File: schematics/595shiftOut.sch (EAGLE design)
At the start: 7 parts, among them IC1 74HC595N, IC2 74HC595N, U1 TINY45-20-DIP

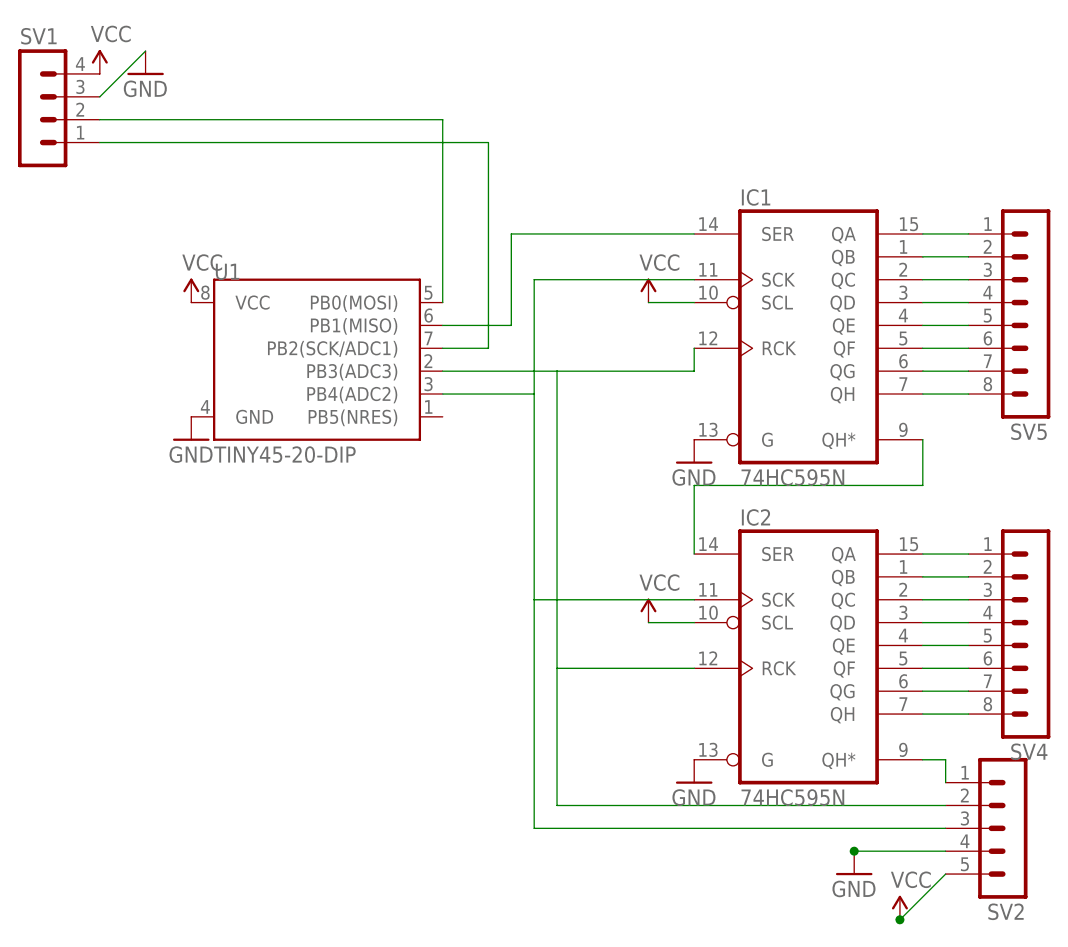
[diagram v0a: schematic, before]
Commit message: rework the schematics for cnc milling
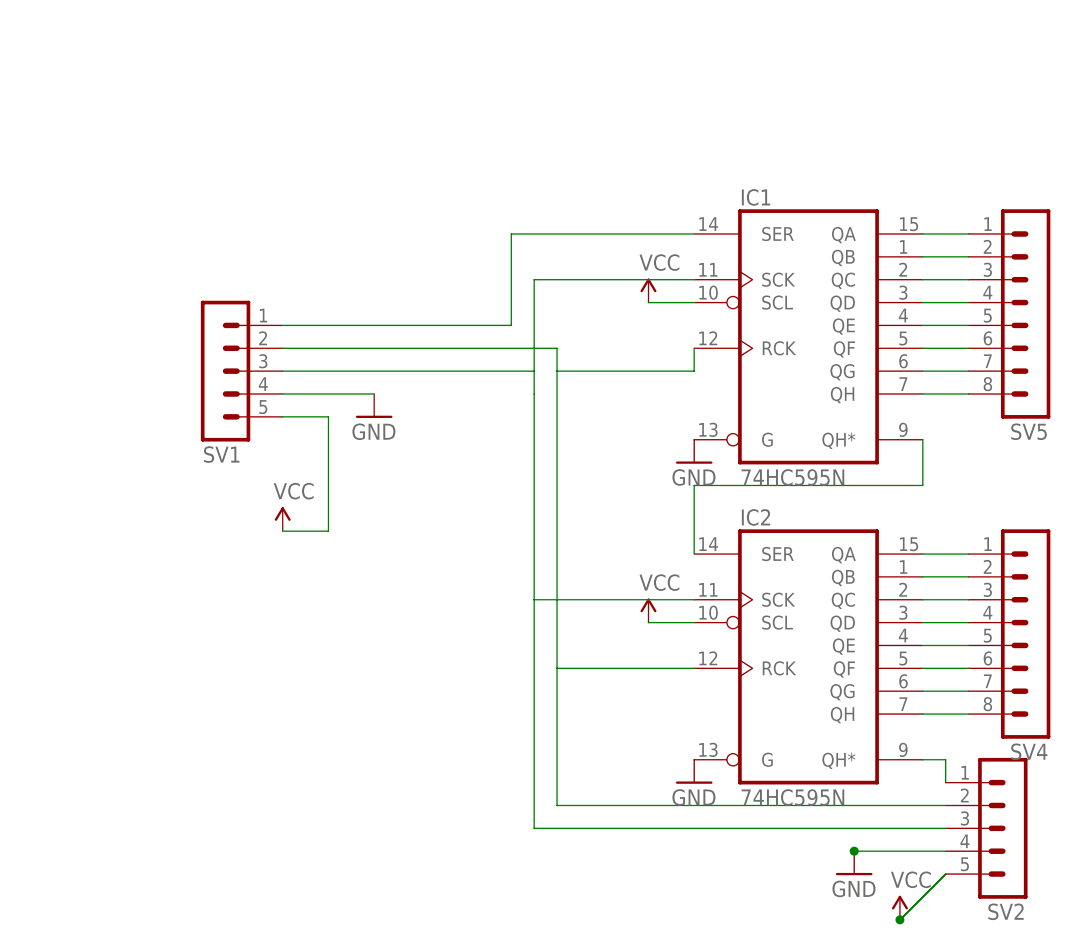
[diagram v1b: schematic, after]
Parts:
- removed U1: TINY45-20-DIP, SparkFun-DigitalIC:ATTINY45TINY45-20-DIP
- SV1: device con-lstb:MA04-1 -> con-lstb:MA05-1
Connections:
- removed net N$1: SV1.2, U1.PB0(MOSI)
- removed net N$2: SV1.1, U1.PB2(SCK/ADC1)
- net GND: now also SV1.4; no longer SV1.3, U1.GND
- net N$3: now also SV1.1; no longer U1.PB1(MISO)
- net N$4: now also SV1.2; no longer U1.PB3(ADC3)
- net N$5: now also SV1.3; no longer U1.PB4(ADC2)
- net VCC: now also SV1.5; no longer SV1.4, U1.VCC
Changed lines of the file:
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@@
 <?xml version="1.0" encoding="utf-8"?>
 <!DOCTYPE eagle SYSTEM "eagle.dtd">
-<eagle version="6.4">
+<eagle version="7.3.0">
 <drawing>
 <settings>
@@
 </classes>
 <parts>
-<part name="U1" library="SparkFun-DigitalIC" deviceset="ATTINY45" device="TINY45-20-DIP" value="TINY45-20-DIP"/>
-<part name="SUPPLY1" library="SparkFun-Aesthetics" deviceset="VCC" device=""/>
-<part name="GND1" library="SparkFun-Aesthetics" deviceset="GND" device=""/>
-<part name="SV1" library="con-lstb" deviceset="MA04-1" device=""/>
-<part name="SUPPLY2" library="SparkFun-Aesthetics" deviceset="VCC" device=""/>
-<part name="GND2" library="SparkFun-Aesthetics" deviceset="GND" device=""/>
 <part name="IC1" library="74xx-eu" deviceset="74*595" device="N" technology="HC"/>
 <part name="IC2" library="74xx-eu" deviceset="74*595" device="N" technology="HC"/>
@@
 <part name="GND5" library="SparkFun-Aesthetics" deviceset="GND" device=""/>
 <part name="SUPPLY5" library="SparkFun-Aesthetics" deviceset="VCC" device=""/>
+<part name="SV1" library="con-lstb" deviceset="MA05-1" device=""/>
+<part name="GND1" library="SparkFun-Aesthetics" deviceset="GND" device=""/>
+<part name="SUPPLY1" library="SparkFun-Aesthetics" deviceset="VCC" device=""/>
 </parts>
 <sheets>
@@
 </plain>
 <instances>
-<instance part="U1" gate="G$1" x="35.56" y="30.48"/>
-<instance part="SUPPLY1" gate="1" x="20.32" y="38.1"/>
-<instance part="GND1" gate="1" x="20.32" y="22.86"/>
-<instance part="SV1" gate="1" x="2.54" y="60.96"/>
-<instance part="SUPPLY2" gate="1" x="10.16" y="63.5"/>
-<instance part="GND2" gate="1" x="15.24" y="63.5"/>
 <instance part="IC1" gate="A" x="88.9" y="35.56"/>
 <instance part="IC2" gate="A" x="88.9" y="0"/>
@@
 <instance part="GND5" gate="1" x="93.98" y="-25.4"/>
 <instance part="SUPPLY5" gate="1" x="99.06" y="-30.48"/>
+<instance part="SV1" gate="G$1" x="22.86" y="30.48" rot="MR180"/>
+<instance part="GND1" gate="1" x="40.64" y="25.4"/>
+<instance part="SUPPLY1" gate="1" x="30.48" y="12.7"/>
 </instances>
 <busses>
@@
 <net name="VCC" class="0">
 <segment>
-<pinref part="U1" gate="G$1" pin="VCC"/>
-<pinref part="SUPPLY1" gate="1" pin="VCC"/>
-</segment>
-<segment>
-<pinref part="SV1" gate="1" pin="4"/>
-<pinref part="SUPPLY2" gate="1" pin="VCC"/>
-</segment>
-<segment>
 <pinref part="IC1" gate="A" pin="SCL"/>
 <pinref part="SUPPLY3" gate="1" pin="VCC"/>
@@
 <pinref part="SUPPLY5" gate="1" pin="VCC"/>
 <wire x1="99.06" y1="-30.48" x2="104.14" y2="-25.4" width="0.1524" layer="91"/>
+<wire x1="99.06" y1="-30.48" x2="104.14" y2="-25.4" width="0.1524" layer="91"/>
+<wire x1="99.06" y1="-30.48" x2="104.14" y2="-25.4" width="0.1524" layer="91"/>
+<wire x1="99.06" y1="-30.48" x2="104.14" y2="-25.4" width="0.1524" layer="91"/>
+</segment>
+<segment>
+<pinref part="SV1" gate="G$1" pin="5"/>
+<wire x1="30.48" y1="25.4" x2="35.56" y2="25.4" width="0.1524" layer="91"/>
+<wire x1="35.56" y1="25.4" x2="35.56" y2="12.7" width="0.1524" layer="91"/>
+<pinref part="SUPPLY1" gate="1" pin="VCC"/>
+<wire x1="35.56" y1="12.7" x2="30.48" y2="12.7" width="0.1524" layer="91"/>
 </segment>
 </net>
 <net name="GND" class="0">
-<segment>
-<pinref part="U1" gate="G$1" pin="GND"/>
-<pinref part="GND1" gate="1" pin="GND"/>
-</segment>
-<segment>
-<pinref part="SV1" gate="1" pin="3"/>
-<pinref part="GND2" gate="1" pin="GND"/>
-<wire x1="15.24" y1="66.04" x2="10.16" y2="60.96" width="0.1524" layer="91"/>
-</segment>
 <segment>
 <pinref part="IC2" gate="A" pin="G"/>
@@
 <wire x1="93.98" y1="-22.86" x2="104.14" y2="-22.86" width="0.1524" layer="91"/>
 </segment>
-</net>
-<net name="N$1" class="0">
-<segment>
-<pinref part="SV1" gate="1" pin="2"/>
-<pinref part="U1" gate="G$1" pin="PB0(MOSI)"/>
-<wire x1="10.16" y1="58.42" x2="48.26" y2="58.42" width="0.1524" layer="91"/>
-<wire x1="48.26" y1="58.42" x2="48.26" y2="38.1" width="0.1524" layer="91"/>
-</segment>
-</net>
-<net name="N$2" class="0">
-<segment>
-<pinref part="SV1" gate="1" pin="1"/>
-<wire x1="10.16" y1="55.88" x2="53.34" y2="55.88" width="0.1524" layer="91"/>
-<wire x1="53.34" y1="55.88" x2="53.34" y2="33.02" width="0.1524" layer="91"/>
-<pinref part="U1" gate="G$1" pin="PB2(SCK/ADC1)"/>
-<wire x1="53.34" y1="33.02" x2="48.26" y2="33.02" width="0.1524" layer="91"/>
+<segment>
+<pinref part="SV1" gate="G$1" pin="4"/>
+<pinref part="GND1" gate="1" pin="GND"/>
+<wire x1="30.48" y1="27.94" x2="40.64" y2="27.94" width="0.1524" layer="91"/>
 </segment>
 </net>
 <net name="N$3" class="0">
 <segment>
-<pinref part="U1" gate="G$1" pin="PB1(MISO)"/>
-<wire x1="48.26" y1="35.56" x2="55.88" y2="35.56" width="0.1524" layer="91"/>
+<wire x1="30.48" y1="35.56" x2="55.88" y2="35.56" width="0.1524" layer="91"/>
 <wire x1="55.88" y1="35.56" x2="55.88" y2="45.72" width="0.1524" layer="91"/>
 <pinref part="IC1" gate="A" pin="SER"/>
 <wire x1="55.88" y1="45.72" x2="76.2" y2="45.72" width="0.1524" layer="91"/>
+<pinref part="SV1" gate="G$1" pin="1"/>
 </segment>
 </net>
 <net name="N$4" class="0">
 <segment>
-<pinref part="U1" gate="G$1" pin="PB3(ADC3)"/>
 <pinref part="IC1" gate="A" pin="RCK"/>
-<wire x1="48.26" y1="30.48" x2="60.96" y2="30.48" width="0.1524" layer="91"/>
+<wire x1="60.96" y1="33.02" x2="60.96" y2="30.48" width="0.1524" layer="91"/>
 <wire x1="60.96" y1="30.48" x2="76.2" y2="30.48" width="0.1524" layer="91"/>
 <wire x1="76.2" y1="30.48" x2="76.2" y2="33.02" width="0.1524" layer="91"/>
@@
 <wire x1="60.96" y1="-17.78" x2="104.14" y2="-17.78" width="0.1524" layer="91"/>
 <pinref part="SV2" gate="G$1" pin="2"/>
+<wire x1="60.96" y1="33.02" x2="30.48" y2="33.02" width="0.1524" layer="91"/>
+<pinref part="SV1" gate="G$1" pin="2"/>
 </segment>
 </net>
 <net name="N$5" class="0">
 <segment>
-<pinref part="U1" gate="G$1" pin="PB4(ADC2)"/>
-<wire x1="48.26" y1="27.94" x2="58.42" y2="27.94" width="0.1524" layer="91"/>
-<wire x1="58.42" y1="27.94" x2="58.42" y2="40.64" width="0.1524" layer="91"/>
+<wire x1="58.42" y1="27.94" x2="58.42" y2="30.48" width="0.1524" layer="91"/>
 <pinref part="IC1" gate="A" pin="SCK"/>
+<wire x1="58.42" y1="30.48" x2="58.42" y2="40.64" width="0.1524" layer="91"/>
 <wire x1="58.42" y1="40.64" x2="76.2" y2="40.64" width="0.1524" layer="91"/>
 <wire x1="58.42" y1="27.94" x2="58.42" y2="5.08" width="0.1524" layer="91"/>
@@
 <wire x1="58.42" y1="-20.32" x2="104.14" y2="-20.32" width="0.1524" layer="91"/>
 <pinref part="SV2" gate="G$1" pin="3"/>
-</segment>
-</net>
+<wire x1="58.42" y1="30.48" x2="30.48" y2="30.48" width="0.1524" layer="91"/>
+<pinref part="SV1" gate="G$1" pin="3"/>
+</segment>
+</net>
